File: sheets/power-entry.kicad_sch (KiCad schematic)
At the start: 47 parts

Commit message: Swap all resistors, capacitors and test points for DropOut parts
Library bumped to 752b63c (PR #22: 83 AEC-Q200 chip resistors and MLCCs,
PR #24: passive symbol layout). Each passive is now a real part, chosen
by rule: exact value and dielectric, tolerance and voltage at least as
good, the drawn package else the next larger, then manufacturer order;
the other built sources stay in the library as alternates.

Where the library has no part in the drawn package: 10nF C0G, 4.7nF C0G,
1uF 16V and 470nF 16V 0402 -> 0603; 68nF C0G, 100nF C0G and 10uF 16V
0805 -> 1206; 32k 1% -> 0.1% (TNPW060332K0BEEA); CCAP 1uF 50V (not built)
-> 1uF 100V 1206. 0R debug links on regulator outputs use the 5 A
CRCW06030000Z0EAHP jumper.

Also fixes test points: f9af1d2 described them as swapped, but they were
still stock symbols. They are now TestPoint_Pad_D1.0mm (signals) and
Harwin S1751-46R (GND loops).

Only placeholders left: L201 / C208 (EMI filter, TBD) and J901-J903.

Co-Authored-By: Claude Opus 5.5 <noreply@anthropic.com>
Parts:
- C: footprint (none) -> DropOut_Capacitor_SMD:C_1206_3216Metric; symbol Device:C -> DropOut_Capacitor:GCM31C5C2A104JE02L; Case (none) -> 1206; DigiKey_PN (none) -> 490-GCM31C5C2A104JE02LCT-ND; MPN (none) -> GCM31C5C2A104JE02L; Manufacturer (none) -> Murata; Mouser_PN (none) -> 81-GCM31C5C2A104JE2L; Package 0805 -> (none); Placeholder PLACEHOLDER: awaiting DropOut_Resistor/DropOut_Capacitor pa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 -> (none); Temperature_Grade (none) -> AEC-Q200, -55 to +125 °C; Tolerance 5% -> ±5%; Voltage 25V -> 100V
- C: footprint (none) -> DropOut_Capacitor_SMD:C_0402_1005Metric; symbol Device:C -> DropOut_Capacitor:GCM155R71C104KA55D; Case (none) -> 0402; DigiKey_PN (none) -> 490-4759-1-ND; MPN (none) -> GCM155R71C104KA55D; Manufacturer (none) -> Murata; Mouser_PN (none) -> 81-GCM155R71C104KA5D; Package 0402 -> (none); Placeholder PLACEHOLDER: awaiting DropOut_Resistor/DropOut_Capacitor pa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 -> (none); Temperature_Grade (none) -> AEC-Q200, -55 to +125 °C; Tolerance 10% -> ±10%
- C: footprint (none) -> DropOut_Capacitor_SMD:C_1206_3216Metric; symbol Device:C -> DropOut_Capacitor:GCM31C5C1H683JA16L; Case (none) -> 1206; DigiKey_PN (none) -> 490-5323-1-ND; MPN (none) -> GCM31C5C1H683JA16L; Manufacturer (none) -> Murata; Mouser_PN (none) -> 81-GCM31C5C1H683JA6L; Notes (none) -> No AEC-Q200 68 nF C0G part exists in the drawn 0805 package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; Package 0805 -> (none); Placeholder PLACEHOLDER: awaiting DropOut_Resistor/DropOut_Capacitor pa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 -> (none); Temperature_Grade (none) -> AEC-Q200, -55 to +125 °C; Tolerance 5% -> ±5%
- C: footprint (none) -> DropOut_Capacitor_SMD:C_1206_3216Metric; symbol Device:C -> DropOut_Capacitor:CGA5L2X7R2A105K160AA; Case (none) -> 1206; DigiKey_PN (none) -> 445-5845-1-ND; MPN (none) -> CGA5L2X7R2A105K160AA; Manufacturer (none) -> TDK; Mouser_PN (none) -> 810-CGA5L2X7R2A105K; Package 0805 -> (none); Placeholder PLACEHOLDER: awaiting DropOut_Resistor/DropOut_Capacitor pa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 -> (none); Temperature_Grade (none) -> AEC-Q200, -55 to +125 °C; Tolerance 10% -> ±10%; Voltage 50V -> 100V
- C: footprint (none) -> DropOut_Capacitor_SMD:C_0603_1608Metric; symbol Device:C -> DropOut_Capacitor:GCM1885C1H103GA16D; Case (none) -> 0603; DigiKey_PN (none) -> 490-GCM1885C1H103GA16DCT-ND; MPN (none) -> GCM1885C1H103GA16D; Manufacturer (none) -> Murata; Mouser_PN (none) -> 81-GCM1885C1H103GA6D; Notes (none) -> No AEC-Q200 part exists in the drawn 0402 package (DigiKey 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; Package 0402 -> (none); Placeholder PLACEHOLDER: awaiting DropOut_Resistor/DropOut_Capacitor pa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 -> (none); Temperature_Grade (none) -> AEC-Q200, -55 to +125 °C; Tolerance 5% -> ±2%
- C: footprint (none) -> DropOut_Capacitor_SMD:C_0603_1608Metric; symbol Device:C -> DropOut_Capacitor:GCJ188R72A104KA01D; Case (none) -> 0603; DigiKey_PN (none) -> 490-13420-1-ND; MPN (none) -> GCJ188R72A104KA01D; Manufacturer (none) -> Murata; Mouser_PN (none) -> 81-GCJ188R72A104KA1D; Notes (none) -> Murata makes no 100 V 100 nF X7R GCM in 0603; GCJ is Murata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; Package 0603 -> (none); Placeholder PLACEHOLDER: awaiting DropOut_Resistor/DropOut_Capacitor pa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 -> (none); Temperature_Grade (none) -> AEC-Q200, -55 to +125 °C; Tolerance 10% -> ±10%
- C: footprint (none) -> DropOut_Capacitor_SMD:C_0603_1608Metric; symbol Device:C -> DropOut_Capacitor:GCM1885C2A103JE02D; Case (none) -> 0603; DigiKey_PN (none) -> 490-GCM1885C2A103JE02DCT-ND; MPN (none) -> GCM1885C2A103JE02D; Manufacturer (none) -> Murata; Mouser_PN (none) -> 81-GCM1885C2A103JE2D; Package 0603 -> (none); Placeholder PLACEHOLDER: awaiting DropOut_Resistor/DropOut_Capacitor pa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 -> (none); Temperature_Grade (none) -> AEC-Q200, -55 to +125 °C; Tolerance 5% -> ±5%
- C: footprint (none) -> DropOut_Capacitor_SMD:C_1210_3225Metric; symbol Device:C -> DropOut_Capacitor:CNA6P1X7R2A475K250AE; Case (none) -> 1210; DigiKey_PN (none) -> 445-181409-1-ND; MPN (none) -> CNA6P1X7R2A475K250AE; Manufacturer (none) -> TDK; Mouser_PN (none) -> 810-CNA6P1X7R2A475K2; Notes (none) -> TDK makes this value only in its CNA soft termination serie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; Package 1210 -> (none); Placeholder PLACEHOLDER: awaiting DropOut_Resistor/DropOut_Capacitor pa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 -> (none); Temperature_Grade (none) -> AEC-Q200, -55 to +125 °C; Tolerance 10% -> ±10%
- R: footprint (none) -> DropOut_Resistor_SMD:R_0603_1608Metric; symbol Device:R -> DropOut_Resistor:AC0603FR-077K87L; Case (none) -> 0603; DigiKey_PN (none) -> 13-AC0603FR-077K87LCT-ND; MPN (none) -> AC0603FR-077K87L; Manufacturer (none) -> Yageo; Mouser_PN (none) -> 603-AC0603FR-077K87L; Package 0603 -> (none); Placeholder PLACEHOLDER: awaiting DropOut_Resistor/DropOut_Capacitor pa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 -> (none); Power (none) -> 1/10W; Temperature_Grade (none) -> AEC-Q200, -55 to +155 °C; Tolerance 1% -> ±1%; Voltage (none) -> 75V
- R: footprint (none) -> DropOut_Resistor_SMD:R_0402_1005Metric; symbol Device:R -> DropOut_Resistor:AC0402JR-0710KL; Case (none) -> 0402; DigiKey_PN (none) -> YAG3517CT-ND; MPN (none) -> AC0402JR-0710KL; Manufacturer (none) -> Yageo; Mouser_PN (none) -> 603-AC0402JR-0710KL; Package 0402 -> (none); Placeholder PLACEHOLDER: awaiting DropOut_Resistor/DropOut_Capacitor pa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 -> (none); Power (none) -> 1/16W; Temperature_Grade (none) -> AEC-Q200, -55 to +155 °C; Tolerance 5% -> ±5%; Voltage (none) -> 50V
- R: footprint (none) -> DropOut_Resistor_SMD:R_0603_1608Metric; symbol Device:R -> DropOut_Resistor:AC0603FR-0749R9L; Case (none) -> 0603; DigiKey_PN (none) -> YAG3611CT-ND; MPN (none) -> AC0603FR-0749R9L; Manufacturer (none) -> Yageo; Mouser_PN (none) -> 603-AC0603FR-0749R9L; Package 0603 -> (none); Placeholder PLACEHOLDER: awaiting DropOut_Resistor/DropOut_Capacitor pa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 -> (none); Power (none) -> 1/10W; Temperature_Grade (none) -> AEC-Q200, -55 to +155 °C; Tolerance 1% -> ±1%; Voltage (none) -> 75V
- R: footprint (none) -> DropOut_Resistor_SMD:R_0603_1608Metric; symbol Device:R -> DropOut_Resistor:TNPW060332K0BEEA; Case (none) -> 0603; DigiKey_PN (none) -> 541-TNPW060332K0BEEACT-ND; MPN (none) -> TNPW060332K0BEEA; Manufacturer (none) -> Vishay; Mouser_PN (none) -> 71-TNPW060332K0BEEA; Notes (none) -> 32 kΩ is an E192 value: no AEC-Q200 1 % thick film part off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; Package 0603 -> (none); Placeholder PLACEHOLDER: awaiting DropOut_Resistor/DropOut_Capacitor pa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 -> (none); Power (none) -> 0.11W; Temperature_Grade (none) -> AEC-Q200, -55 to +175 °C; Tolerance 1% -> ±0.1%; Voltage (none) -> 100V
- R: footprint (none) -> DropOut_Resistor_SMD:R_0603_1608Metric; symbol Device:R -> DropOut_Resistor:AC0603FR-072KL; Case (none) -> 0603; DigiKey_PN (none) -> YAG3590CT-ND; MPN (none) -> AC0603FR-072KL; Manufacturer (none) -> Yageo; Mouser_PN (none) -> 603-AC0603FR-072KL; Package 0603 -> (none); Placeholder PLACEHOLDER: awaiting DropOut_Resistor/DropOut_Capacitor pa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 -> (none); Power (none) -> 1/10W; Temperature_Grade (none) -> AEC-Q200, -55 to +155 °C; Tolerance 1% -> ±1%; Voltage (none) -> 75V
- R: footprint (none) -> DropOut_Resistor_SMD:R_0402_1005Metric; symbol Device:R -> DropOut_Resistor:AC0402JR-070RL; Case (none) -> 0402; DigiKey_PN (none) -> 311-0.0LBCT-ND; MPN (none) -> AC0402JR-070RL; Manufacturer (none) -> Yageo; Mouser_PN (none) -> 603-AC0402JR-070RL; Package 0402 -> (none); Placeholder PLACEHOLDER: awaiting DropOut_Resistor/DropOut_Capacitor pa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 -> (none); Temperature_Grade (none) -> AEC-Q200, -55 to +155 °C; Tolerance 5% -> (none)
- R: footprint (none) -> DropOut_Resistor_SMD:R_0603_1608Metric; symbol Device:R -> DropOut_Resistor:AC0603FR-07107KL; Case (none) -> 0603; DigiKey_PN (none) -> 13-AC0603FR-07107KLCT-ND; MPN (none) -> AC0603FR-07107KL; Manufacturer (none) -> Yageo; Mouser_PN (none) -> 603-AC0603FR-07107KL; Package 0603 -> (none); Placeholder PLACEHOLDER: awaiting DropOut_Resistor/DropOut_Capacitor pa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 -> (none); Power (none) -> 1/10W; Temperature_Grade (none) -> AEC-Q200, -55 to +155 °C; Tolerance 1% -> ±1%; Voltage (none) -> 75V
- R: footprint (none) -> DropOut_Resistor_SMD:R_0402_1005Metric; symbol Device:R -> DropOut_Resistor:AC0402JR-0710RL; Case (none) -> 0402; DigiKey_PN (none) -> YAG3519CT-ND; MPN (none) -> AC0402JR-0710RL; Manufacturer (none) -> Yageo; Mouser_PN (none) -> 603-AC0402JR-0710RL; Package 0402 -> (none); Placeholder PLACEHOLDER: awaiting DropOut_Resistor/DropOut_Capacitor pa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 -> (none); Power (none) -> 1/16W; Temperature_Grade (none) -> AEC-Q200, -55 to +155 °C; Tolerance 5% -> ±5%; Voltage (none) -> 50V
- R: footprint (none) -> DropOut_Resistor_SMD:R_0603_1608Metric; symbol Device:R -> DropOut_Resistor:AC0603FR-072K1L; Case (none) -> 0603; DigiKey_PN (none) -> 13-AC0603FR-072K1LCT-ND; MPN (none) -> AC0603FR-072K1L; Manufacturer (none) -> Yageo; Mouser_PN (none) -> 603-AC0603FR-072K1L; Package 0603 -> (none); Placeholder PLACEHOLDER: awaiting DropOut_Resistor/DropOut_Capacitor pa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 -> (none); Power (none) -> 1/10W; Temperature_Grade (none) -> AEC-Q200, -55 to +155 °C; Tolerance 1% -> ±1%; Voltage (none) -> 75V
- R: footprint (none) -> DropOut_Resistor_SMD:R_0603_1608Metric; symbol Device:R -> DropOut_Resistor:ERA-3AEB103V; Case (none) -> 0603; DigiKey_PN (none) -> P10KDBCT-ND; MPN (none) -> ERA-3AEB103V; Manufacturer (none) -> Panasonic; Mouser_PN (none) -> 667-ERA-3AEB103V; Notes (none) -> Precision part: not substitutable (0.1 %, ±25 ppm/K thin fi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; Package 0603 -> (none); Placeholder PLACEHOLDER: awaiting DropOut_Resistor/DropOut_Capacitor pa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 -> (none); Power (none) -> 0.1W; Tempco 25ppm -> (none); Temperature_Grade (none) -> AEC-Q200, -55 to +155 °C; Tolerance 0.1% -> ±0.1%; Voltage (none) -> 75V
- TP: value TP_LM_FLT_L -> TestPoint_Pad_D1.0mm; footprint (none) -> DropOut_TestPoint:TestPoint_Pad_D1.0mm; symbol Connector:TestPoint -> DropOut_Connector:TestPoint_Pad_D1.0mm; DigiKey_PN (none) -> -; MPN (none) -> TestPoint_Pad_D1.0mm; Manufacturer (none) -> DropOut; Mouser_PN (none) -> -; Notes (none) -> PCB copper only; nothing to order. Excluded from BOM and po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; Placeholder PLACEHOLDER: awaiting DropOut test-point part (library brie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 -> (none); Type 1mm pad -> (none)
- TP: value TP_BATT_MON -> TestPoint_Pad_D1.0mm; footprint (none) -> DropOut_TestPoint:TestPoint_Pad_D1.0mm; symbol Connector:TestPoint -> DropOut_Connector:TestPoint_Pad_D1.0mm; DigiKey_PN (none) -> -; MPN (none) -> TestPoint_Pad_D1.0mm; Manufacturer (none) -> DropOut; Mouser_PN (none) -> -; Notes (none) -> PCB copper only; nothing to order. Excluded from BOM and po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; Placeholder PLACEHOLDER: awaiting DropOut test-point part (library brie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 -> (none); Type 1mm pad -> (none)
- TP: value TP_VBAT_Q2D -> TestPoint_Pad_D1.0mm; footprint (none) -> DropOut_TestPoint:TestPoint_Pad_D1.0mm; symbol Connector:TestPoint -> DropOut_Connector:TestPoint_Pad_D1.0mm; DigiKey_PN (none) -> -; MPN (none) -> TestPoint_Pad_D1.0mm; Manufacturer (none) -> DropOut; Mouser_PN (none) -> -; Notes (none) -> PCB copper only; nothing to order. Excluded from BOM and po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; Placeholder PLACEHOLDER: awaiting DropOut test-point part (library brie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 -> (none); Type 1mm pad -> (none)
- TP: value TP_INH -> TestPoint_Pad_D1.0mm; footprint (none) -> DropOut_TestPoint:TestPoint_Pad_D1.0mm; symbol Connector:TestPoint -> DropOut_Connector:TestPoint_Pad_D1.0mm; DigiKey_PN (none) -> -; MPN (none) -> TestPoint_Pad_D1.0mm; Manufacturer (none) -> DropOut; Mouser_PN (none) -> -; Notes (none) -> PCB copper only; nothing to order. Excluded from BOM and po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; Placeholder PLACEHOLDER: awaiting DropOut test-point part (library brie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 -> (none); Type 1mm pad -> (none)
- TP: value TP_VBAT_D -> TestPoint_Pad_D1.0mm; footprint (none) -> DropOut_TestPoint:TestPoint_Pad_D1.0mm; symbol Connector:TestPoint -> DropOut_Connector:TestPoint_Pad_D1.0mm; DigiKey_PN (none) -> -; MPN (none) -> TestPoint_Pad_D1.0mm; Manufacturer (none) -> DropOut; Mouser_PN (none) -> -; Notes (none) -> PCB copper only; nothing to order. Excluded from BOM and po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; Placeholder PLACEHOLDER: awaiting DropOut test-point part (library brie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 -> (none); Type 1mm pad -> (none)
- TP: value TP_GND -> S1751-46R; footprint (none) -> DropOut_TestPoint:TestPoint_Harwin_S1751; symbol Connector:TestPoint -> DropOut_Connector:S1751-46R; DigiKey_PN (none) -> 952-1478-1-ND; MPN (none) -> S1751-46R; Manufacturer (none) -> Harwin; Mouser_PN (none) -> 855-S1751-46R; Notes (none) -> Ground test point (probe loop) for a scope ground spring or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; Placeholder PLACEHOLDER: awaiting DropOut test-point part (library brie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 -> (none); Temperature_Grade (none) -> -55 to +125 °C; Type probe loop -> (none)
- TP: value TP_VBAT_FILT -> TestPoint_Pad_D1.0mm; footprint (none) -> DropOut_TestPoint:TestPoint_Pad_D1.0mm; symbol Connector:TestPoint -> DropOut_Connector:TestPoint_Pad_D1.0mm; DigiKey_PN (none) -> -; MPN (none) -> TestPoint_Pad_D1.0mm; Manufacturer (none) -> DropOut; Mouser_PN (none) -> -; Notes (none) -> PCB copper only; nothing to order. Excluded from BOM and po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; Placeholder PLACEHOLDER: awaiting DropOut test-point part (library brie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 -> (none); Type 1mm pad -> (none)
- TP: value TP_VBAT_PROT -> TestPoint_Pad_D1.0mm; footprint (none) -> DropOut_TestPoint:TestPoint_Pad_D1.0mm; symbol Connector:TestPoint -> DropOut_Connector:TestPoint_Pad_D1.0mm; DigiKey_PN (none) -> -; MPN (none) -> TestPoint_Pad_D1.0mm; Manufacturer (none) -> DropOut; Mouser_PN (none) -> -; Notes (none) -> PCB copper only; nothing to order. Excluded from BOM and po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; Placeholder PLACEHOLDER: awaiting DropOut test-point part (library brie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 -> (none); Type 1mm pad -> (none)
- TP: value TP_VBAT_IN -> TestPoint_Pad_D1.0mm; footprint (none) -> DropOut_TestPoint:TestPoint_Pad_D1.0mm; symbol Connector:TestPoint -> DropOut_Connector:TestPoint_Pad_D1.0mm; DigiKey_PN (none) -> -; MPN (none) -> TestPoint_Pad_D1.0mm; Manufacturer (none) -> DropOut; Mouser_PN (none) -> -; Notes (none) -> PCB copper only; nothing to order. Excluded from BOM and po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; Placeholder PLACEHOLDER: awaiting DropOut test-point part (library brie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 -> (none); Type 1mm pad -> (none)

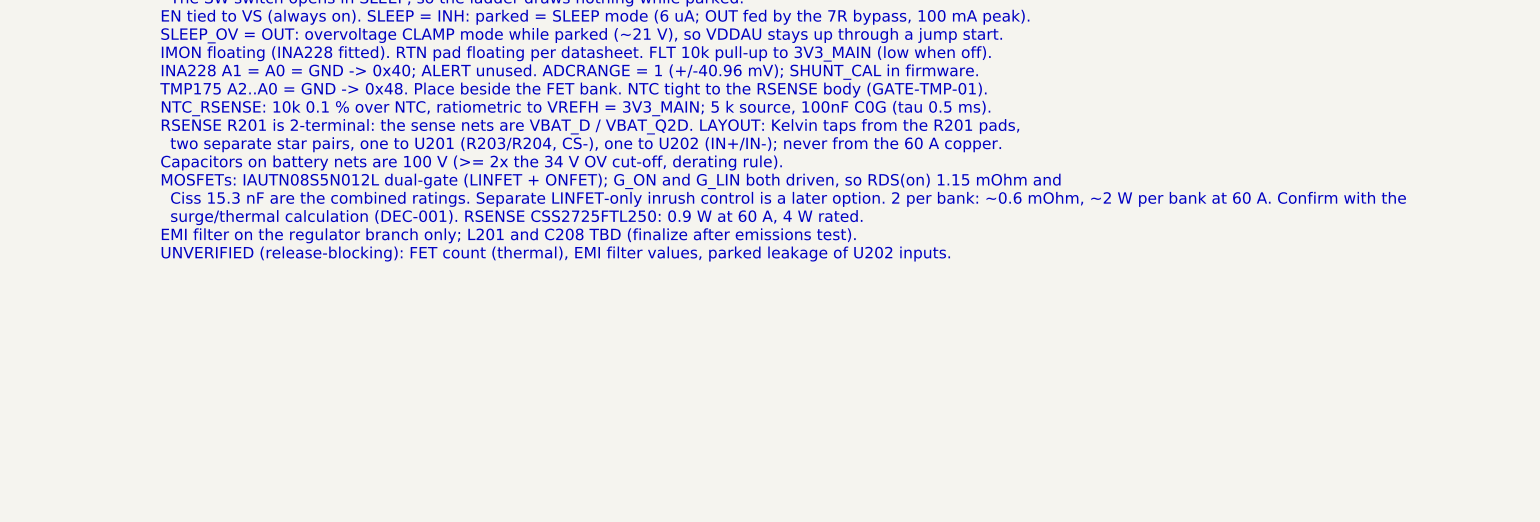
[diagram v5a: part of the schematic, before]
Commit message: Schematic: LHI to the MCU, current notes, net-name map
- LHI on all three TPS2HCS08 is now SW_LHI from S32K344 PTE4 (the
  architecture's GPIO list), still held low by the 10k pull-downs
  through reset.
- Page 4 cites NXP HDG Rev E2 Table 33 for unused GPIO, EXTAL/XTAL and
  the RESET_B pull-up instead of an open 'confirm' note.
- Copper notes for the 10 A output paths (p6) and the 60 A path (p2,
  p9), as IPC-2221 starting estimates to confirm with IPC-2152.
- interfaces.mdx maps the architecture's signal names to the schematic
  nets (RESET_L, T1S_IRQ_L, *_FLT_L, SPI4/SPI2/I2C0 buses).

Co-Authored-By: Claude Opus 5.5 <noreply@anthropic.com>
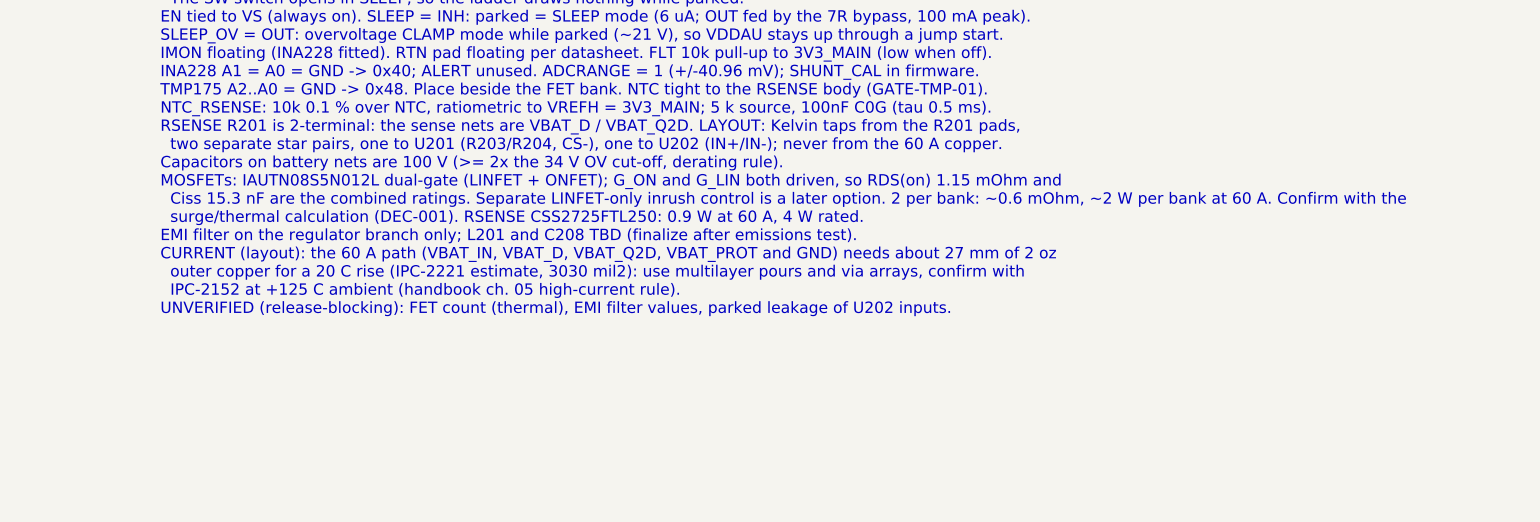
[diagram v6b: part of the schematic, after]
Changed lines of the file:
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@@
 		)
 	)
-	(text "DESIGN VALUES (LM74910H-Q1 SNOSDE6C sec. 9.2; Node60 DEC-001). Values per DropOut D-45.\nR(ILIM) = 12 x RSET / (RSENSE x ILIM) = 12 x 49.9 / (0.25m x 32k) = 74.9 A breaker (Rev A: 75 A).\n  RSET 49.9R: E96 value nearest the 50R in Rev A (50-100R allowed). R(ILIM) 32k: E192, 1 %.\nFast SCP: ISCP to the R201 VBAT_D pad through R204 0R (no RISCP shift) -> 20 mV default = 80 A.\n  R204 keeps the RISCP option (VSNS_SCP = 10.5 uA x RISCP + 20 mV); C212 is the DNP deglitch option (D-48).\nCTMR 68nF C0G: T(OC) = 1.2 x 68n / 82.3u = 0.99 ms; retry = 22.7e6 x 68n = 1.5 s. Tune vs inrush (GATE-PWR-01).\nCCAP 1uF 50V: >= 10 x sum(Ciss) = 10 x 4 x 15.3 nF = 0.61 uF for 4 x IAUTN08S5N012L. CVS 100nF 100V.\nRG 10R + Cdvdt 10nF on HGATE: inrush slew = 55 uA / 10 nF = 5.5 V/ms.\nOV/UV/BATT_MON ladder, 118.97k total (< 120k leakage rule), 1 %:\n  OV rising = 0.60 V x 118.97k / 2.1k  = 34.0 V   (disconnects above 34 V; passes 24 V jump start)\n  UVLO fall = 0.55 V x 118.97k / 11.97k = 5.47 V  (rising 0.60 V -> 5.96 V)\n  BATT_MON = SW x 9.97k / 118.97k = SW / 11.93 (1:12 concept); 3.3 V full scale = 39.4 V\n  BATT_MON source 9.1 k with 10nF C0G (tau 91 us): set the ADC sample time from this.\n  The SW switch opens in SLEEP, so the ladder draws nothing while parked.\nEN tied to VS (always on). SLEEP = INH: parked = SLEEP mode (6 uA; OUT fed by the 7R bypass, 100 mA peak).\nSLEEP_OV = OUT: overvoltage CLAMP mode while parked (~21 V), so VDDAU stays up through a jump start.\nIMON floating (INA228 fitted). RTN pad floating per datasheet. FLT 10k pull-up to 3V3_MAIN (low when off).\nINA228 A1 = A0 = GND -> 0x40; ALERT unused. ADCRANGE = 1 (+/-40.96 mV); SHUNT_CAL in firmware.\nTMP175 A2..A0 = GND -> 0x48. Place beside the FET bank. NTC tight to the RSENSE body (GATE-TMP-01).\nNTC_RSENSE: 10k 0.1 % over NTC, ratiometric to VREFH = 3V3_MAIN; 5 k source, 100nF C0G (tau 0.5 ms).\nRSENSE R201 is 2-terminal: the sense nets are VBAT_D / VBAT_Q2D. LAYOUT: Kelvin taps from the R201 pads,\n  two separate star pairs, one to U201 (R203/R204, CS-), one to U202 (IN+/IN-); never from the 60 A copper.\nCapacitors on battery nets are 100 V (>= 2x the 34 V OV cut-off, derating rule).\nMOSFETs: IAUTN08S5N012L dual-gate (LINFET + ONFET); G_ON and G_LIN both driven, so RDS(on) 1.15 mOhm and\n  Ciss 15.3 nF are the combined ratings. Separate LINFET-only inrush control is a later option. 2 per bank: ~0.6 mOhm, ~2 W per bank at 60 A. Confirm with the\n  surge/thermal calculation (DEC-001). RSENSE CSS2725FTL250: 0.9 W at 60 A, 4 W rated.\nEMI filter on the regulator branch only; L201 and C208 TBD (finalize after emissions test).\nUNVERIFIED (release-blocking): FET count (thermal), EMI filter values, parked leakage of U202 inputs.\n"
+	(text "DESIGN VALUES (LM74910H-Q1 SNOSDE6C sec. 9.2; Node60 DEC-001). Values per DropOut D-45.\nR(ILIM) = 12 x RSET / (RSENSE x ILIM) = 12 x 49.9 / (0.25m x 32k) = 74.9 A breaker (Rev A: 75 A).\n  RSET 49.9R: E96 value nearest the 50R in Rev A (50-100R allowed). R(ILIM) 32k: E192, 1 %.\nFast SCP: ISCP to the R201 VBAT_D pad through R204 0R (no RISCP shift) -> 20 mV default = 80 A.\n  R204 keeps the RISCP option (VSNS_SCP = 10.5 uA x RISCP + 20 mV); C212 is the DNP deglitch option (D-48).\nCTMR 68nF C0G: T(OC) = 1.2 x 68n / 82.3u = 0.99 ms; retry = 22.7e6 x 68n = 1.5 s. Tune vs inrush (GATE-PWR-01).\nCCAP 1uF 50V: >= 10 x sum(Ciss) = 10 x 4 x 15.3 nF = 0.61 uF for 4 x IAUTN08S5N012L. CVS 100nF 100V.\nRG 10R + Cdvdt 10nF on HGATE: inrush slew = 55 uA / 10 nF = 5.5 V/ms.\nOV/UV/BATT_MON ladder, 118.97k total (< 120k leakage rule), 1 %:\n  OV rising = 0.60 V x 118.97k / 2.1k  = 34.0 V   (disconnects above 34 V; passes 24 V jump start)\n  UVLO fall = 0.55 V x 118.97k / 11.97k = 5.47 V  (rising 0.60 V -> 5.96 V)\n  BATT_MON = SW x 9.97k / 118.97k = SW / 11.93 (1:12 concept); 3.3 V full scale = 39.4 V\n  BATT_MON source 9.1 k with 10nF C0G (tau 91 us): set the ADC sample time from this.\n  The SW switch opens in SLEEP, so the ladder draws nothing while parked.\nEN tied to VS (always on). SLEEP = INH: parked = SLEEP mode (6 uA; OUT fed by the 7R bypass, 100 mA peak).\nSLEEP_OV = OUT: overvoltage CLAMP mode while parked (~21 V), so VDDAU stays up through a jump start.\nIMON floating (INA228 fitted). RTN pad floating per datasheet. FLT 10k pull-up to 3V3_MAIN (low when off).\nINA228 A1 = A0 = GND -> 0x40; ALERT unused. ADCRANGE = 1 (+/-40.96 mV); SHUNT_CAL in firmware.\nTMP175 A2..A0 = GND -> 0x48. Place beside the FET bank. NTC tight to the RSENSE body (GATE-TMP-01).\nNTC_RSENSE: 10k 0.1 % over NTC, ratiometric to VREFH = 3V3_MAIN; 5 k source, 100nF C0G (tau 0.5 ms).\nRSENSE R201 is 2-terminal: the sense nets are VBAT_D / VBAT_Q2D. LAYOUT: Kelvin taps from the R201 pads,\n  two separate star pairs, one to U201 (R203/R204, CS-), one to U202 (IN+/IN-); never from the 60 A copper.\nCapacitors on battery nets are 100 V (>= 2x the 34 V OV cut-off, derating rule).\nMOSFETs: IAUTN08S5N012L dual-gate (LINFET + ONFET); G_ON and G_LIN both driven, so RDS(on) 1.15 mOhm and\n  Ciss 15.3 nF are the combined ratings. Separate LINFET-only inrush control is a later option. 2 per bank: ~0.6 mOhm, ~2 W per bank at 60 A. Confirm with the\n  surge/thermal calculation (DEC-001). RSENSE CSS2725FTL250: 0.9 W at 60 A, 4 W rated.\nEMI filter on the regulator branch only; L201 and C208 TBD (finalize after emissions test).\nCURRENT (layout): the 60 A path (VBAT_IN, VBAT_D, VBAT_Q2D, VBAT_PROT and GND) needs about 27 mm of 2 oz\n  outer copper for a 20 C rise (IPC-2221 estimate, 3030 mil2): use multilayer pours and via arrays, confirm with\n  IPC-2152 at +125 C ambient (handbook ch. 05 high-current rule).\nUNVERIFIED (release-blocking): FET count (thermal), EMI filter values, parked leakage of U202 inputs.\n"
 		(exclude_from_sim no)
 		(at 358.14 266.7 0)

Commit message: Pin DropOut library to main 618de03 (PR #35 merged)
The re-pin also brings library PRs #31, #33 and #34 (manufacturer names,
ATM13 Notes, catalog data). Their field changes are copied into the
schematic so every placed symbol matches the library: "Amphenol Sine
Systems", "Stackpole Electronics", "Murata", and the full ATM13 Notes.

Co-Authored-By: Claude Opus 5.5 <noreply@anthropic.com>
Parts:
- RT: Manufacturer Murata Electronics -> Murata
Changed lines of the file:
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@@
 			)
 		)
-		(property "Manufacturer" "Murata Electronics"
+		(property "Manufacturer" "Murata"
 			(at 476.25 203.2 0)
 			(effects
